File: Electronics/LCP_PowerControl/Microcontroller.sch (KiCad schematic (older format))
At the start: 22 parts, among them J4 Conn_02x02_Odd_Even, J5 Conn_02x05_Odd_Even, J6 Conn_02x06_Odd_Even, J7 Conn_02x02_Odd_Even, J8 Conn_02x02_Odd_Even, SW1 SW_Push, U3 MSP430FR5989, Y1 32.768kHz

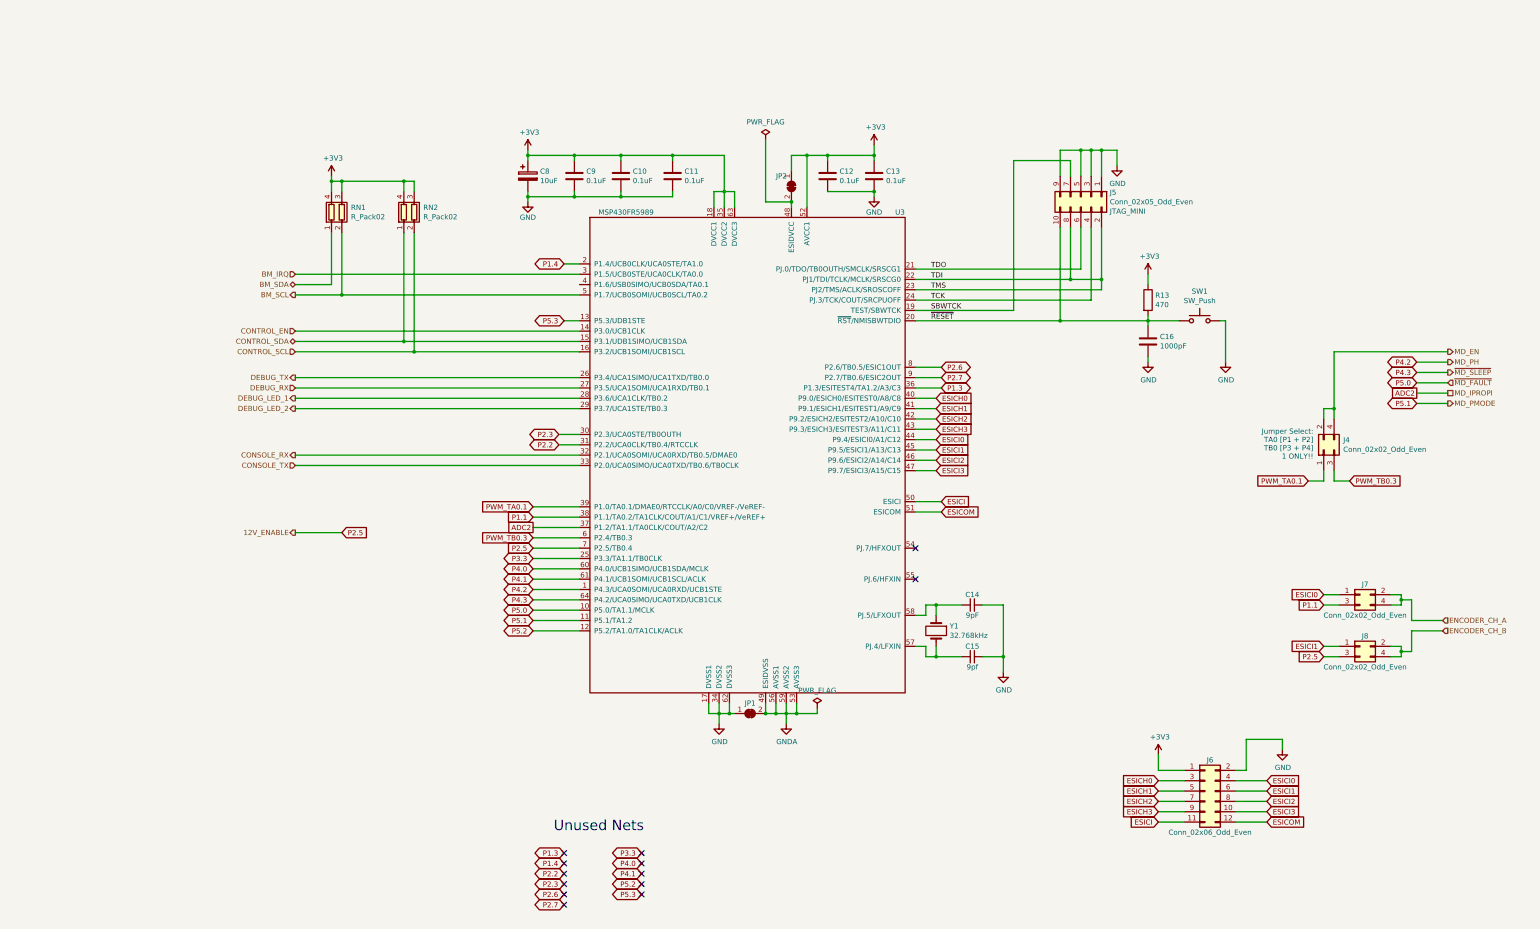
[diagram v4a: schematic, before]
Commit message: Rev1
Removed test points. Cleaned up unnecessary traces. Fixed electrical issues #1-#7
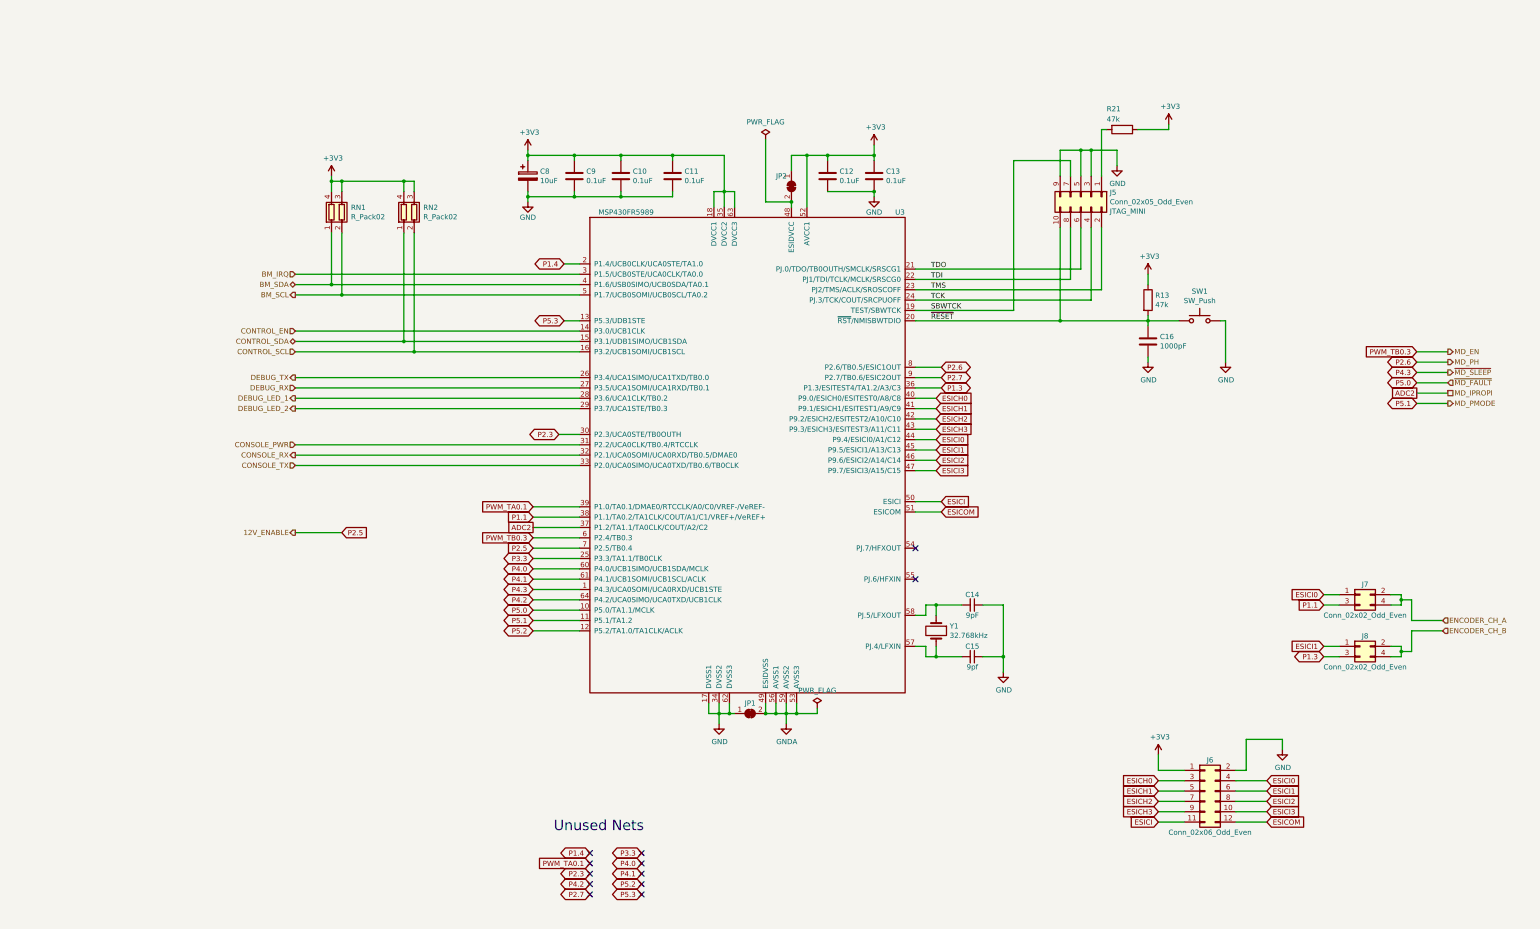
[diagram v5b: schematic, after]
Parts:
- removed J4: Conn_02x02_Odd_Even, Connector_PinHeader_2.00mm:PinHeader_2x02_P2.00mm_Vertical, symbol Connector_Generic:Conn_02x02_Odd_Even
- added R21: 47k, Resistor_SMD:R_0805_2012Metric, symbol Device:R
- R13: value 470 -> 47k; MPN CRGCQ0805F470R -> CRGCQ0805F47K
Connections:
- net +3V3: now also R21.1
- net BM_SDA: now also U3.4 (P1.6/USB0SIMO/UCB0SDA/TA0.1)
- net GND: no longer J5.1 (Pin_1)
- net P1.3: now also J8.3 (Pin_3)
- net P2.5: no longer J8.3 (Pin_3)
- net P4.2: now also U3.64 (P4.2/UCA0SIMO/UCA0TXD/UCB1CLK); no longer U3.1 (P4.3/UCA0SOMI/UCA0RXD/UCB1STE)
- net P4.3: now also U3.1 (P4.3/UCA0SOMI/UCA0RXD/UCB1STE); no longer U3.64 (P4.2/UCA0SIMO/UCA0TXD/UCB1CLK)
- net TDI: no longer J5.2 (Pin_2), U3.23 (PJ2/TMS/ACLK/SROSCOFF)
- net P2.2 renamed CONSOLE_PWR
- new net: J5.1 (Pin_1), R21.2
- new net TMS: J5.2 (Pin_2), U3.23 (PJ2/TMS/ACLK/SROSCOFF)
- no-connect marks 13 -> 12
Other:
- note removed: "Jumper Select:\nTA0 [P1 + P2]\nTB0 [P3 + P4]\n1 ONLY!!"
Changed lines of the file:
@@
 	11850 1850 11850 2000
-Wire Wire Line
-	11700 2100 11700 1850
-Connection ~ 11700 1850
-Wire Wire Line
-	11700 1850 11850 1850
 Wire Wire Line
 	11600 2100 11600 1850
@@
 	11300 1850 11500 1850
 Connection ~ 11600 1850
-Wire Wire Line
-	11600 1850 11700 1850
 Connection ~ 11500 1850
 Wire Wire Line
@@
 P 12150 3300
 F 0 "R13" H 12220 3346 50  0000 L CNN
-F 1 "470" H 12220 3255 50  0000 L CNN
+F 1 "47k" H 12220 3255 50  0000 L CNN
 F 2 "Resistor_SMD:R_0805_2012Metric" V 12080 3300 50  0001 C CNN
 F 3 "~" H 12150 3300 50  0001 C CNN
-F 4 "CRGCQ0805F470R" H 12150 3300 50  0001 C CNN "MPN"
+F 4 "CRGCQ0805F47K" H 12150 3300 50  0001 C CNN "MPN"
 	1    12150 3300
 	1    0    0    -1
@@
 Text GLabel 6200 6000 0    50   BiDi ~ 0
 P4.1
+Text GLabel 6200 6200 0    50   BiDi ~ 0
+P4.2
 Text GLabel 6200 6100 0    50   BiDi ~ 0
-P4.2
-Text GLabel 6200 6200 0    50   BiDi ~ 0
 P4.3
 Wire Wire Line
@@
 Wire Wire Line
 	6200 6300 6650 6300
-Text GLabel 14750 3900 0    50   BiDi ~ 0
+Text GLabel 6750 8950 0    50   BiDi ~ 0
 P4.2
 Wire Wire Line
@@
 Wire Wire Line
 	6200 5500 6650 5500
-Wire Wire Line
-	13850 4350 13950 4350
-Connection ~ 13950 4350
-Wire Wire Line
-	13950 3800 13950 4350
-Wire Wire Line
-	13950 3800 15050 3800
-Text GLabel 13700 5050 0    50   Input ~ 0
-PWM_TA0.1
-Wire Wire Line
-	13700 5050 13850 5050
-Wire Wire Line
-	13850 5050 13850 4950
-$Comp
-L Connector_Generic:Conn_02x02_Odd_Even J4
-U 1 1 5EFC98B3
-P 13850 4750
-F 0 "J4" V 13946 4562 50  0000 R CNN
-F 1 "Conn_02x02_Odd_Even" V 13855 4562 50  0000 R CNN
-F 2 "Connector_PinHeader_2.00mm:PinHeader_2x02_P2.00mm_Vertical" H 13850 4750 50  0001 C CNN
-F 3 "~" H 13850 4750 50  0001 C CNN
-	1    13850 4750
-	0    -1   -1   0
-$EndComp
-Wire Wire Line
-	13950 4350 13950 4450
-Wire Wire Line
-	13850 4350 13850 4450
-Text GLabel 14100 5050 2    50   Input ~ 0
+Text GLabel 14750 3800 0    50   Input ~ 0
 PWM_TB0.3
-Wire Wire Line
-	14100 5050 13950 5050
-Wire Wire Line
-	13950 5050 13950 4950
-Text Notes 13750 4850 2    50   ~ 0
-Jumper Select:\nTA0 [P1 + P2]\nTB0 [P3 + P4]\n1 ONLY!!
 Text GLabel 14750 4200 0    50   UnSpc ~ 0
 ADC2
@@
 Wire Wire Line
 	13850 6250 14000 6250
-Text GLabel 13850 6750 0    50   Input ~ 0
-P2.5
-Wire Wire Line
-	13850 6750 14000 6750
 Text GLabel 4350 5550 2    50   Input ~ 0
 P2.5
@@
 Text GLabel 7250 9050 0    50   BiDi ~ 0
 P5.3
-Text GLabel 6500 8750 0    50   BiDi ~ 0
+Text GLabel 6750 8650 0    50   BiDi ~ 0
 P1.4
 Text GLabel 10150 3950 2    50   BiDi ~ 0
@@
 Wire Wire Line
 	10150 3950 9900 3950
-Text GLabel 6500 9050 0    50   BiDi ~ 0
+Text GLabel 14750 3900 0    50   BiDi ~ 0
 P2.6
-Text GLabel 6500 9150 0    50   BiDi ~ 0
+Text GLabel 6750 9050 0    50   BiDi ~ 0
 P2.7
-Text GLabel 6500 8650 0    50   BiDi ~ 0
+Text GLabel 13850 6750 0    50   BiDi ~ 0
 P1.3
-Text GLabel 6450 4700 0    50   BiDi ~ 0
-P2.2
 Text GLabel 6450 4600 0    50   BiDi ~ 0
 P2.3
 Wire Wire Line
 	6650 4600 6450 4600
-Wire Wire Line
-	6650 4700 6450 4700
-Text GLabel 6500 8850 0    50   BiDi ~ 0
-P2.2
-Text GLabel 6500 8950 0    50   BiDi ~ 0
+Text GLabel 6750 8850 0    50   BiDi ~ 0
 P2.3
 Text GLabel 6200 5800 0    50   BiDi ~ 0
@@
 Text GLabel 7250 8650 0    50   BiDi ~ 0
 P3.3
-NoConn ~ 6500 8650
-NoConn ~ 6500 8750
-NoConn ~ 6500 8850
-NoConn ~ 6500 8950
-NoConn ~ 6500 9050
-NoConn ~ 6500 9150
+NoConn ~ 6750 8650
+NoConn ~ 6750 8850
+NoConn ~ 6750 8950
+NoConn ~ 6750 9050
 NoConn ~ 7250 9050
 NoConn ~ 7250 8950
@@
 Connection ~ 8750 7300
 Wire Wire Line
-	11700 3100 11700 2600
-Wire Wire Line
-	11700 3200 11700 3100
-Connection ~ 11700 3100
-Connection ~ 11400 3100
-Wire Wire Line
-	11400 3100 11700 3100
+	11700 3200 11700 2600
+Wire Wire Line
+	11600 1850 11850 1850
+$Comp
+L Device:R R21
+U 1 1 5FE87C7E
+P 11900 1650
+F 0 "R21" V 11700 1500 50  0000 L CNN
+F 1 "47k" V 11800 1500 50  0000 L CNN
+F 2 "Resistor_SMD:R_0805_2012Metric" V 11830 1650 50  0001 C CNN
+F 3 "~" H 11900 1650 50  0001 C CNN
+F 4 "CRGCQ0805F470R" H 11900 1650 50  0001 C CNN "MPN"
+	1    11900 1650
+	0    1    1    0
+$EndComp
+Wire Wire Line
+	11750 1650 11700 1650
+Wire Wire Line
+	11700 1650 11700 2100
+$Comp
+L power:+3V3 #PWR015
+U 1 1 5FE93D4D
+P 12350 1600
+F 0 "#PWR015" H 12350 1450 50  0001 C CNN
+F 1 "+3V3" H 12365 1773 50  0000 C CNN
+F 2 "" H 12350 1600 50  0001 C CNN
+F 3 "" H 12350 1600 50  0001 C CNN
+	1    12350 1600
+	1    0    0    -1
+$EndComp
+Wire Wire Line
+	12050 1650 12350 1650
+Wire Wire Line
+	12350 1650 12350 1600
+Wire Wire Line
+	3900 4700 6650 4700
+Wire Wire Line
+	6650 3150 4250 3150
+Connection ~ 4250 3150
+Wire Wire Line
+	13850 6750 14000 6750
+Wire Wire Line
+	14750 3800 15050 3800
+Text HLabel 3900 4700 0    50   Input ~ 0
+CONSOLE_PWR
+Text GLabel 6750 8750 0    50   Input ~ 0
+PWM_TA0.1
+NoConn ~ 6750 8750
 $EndSCHEMATC

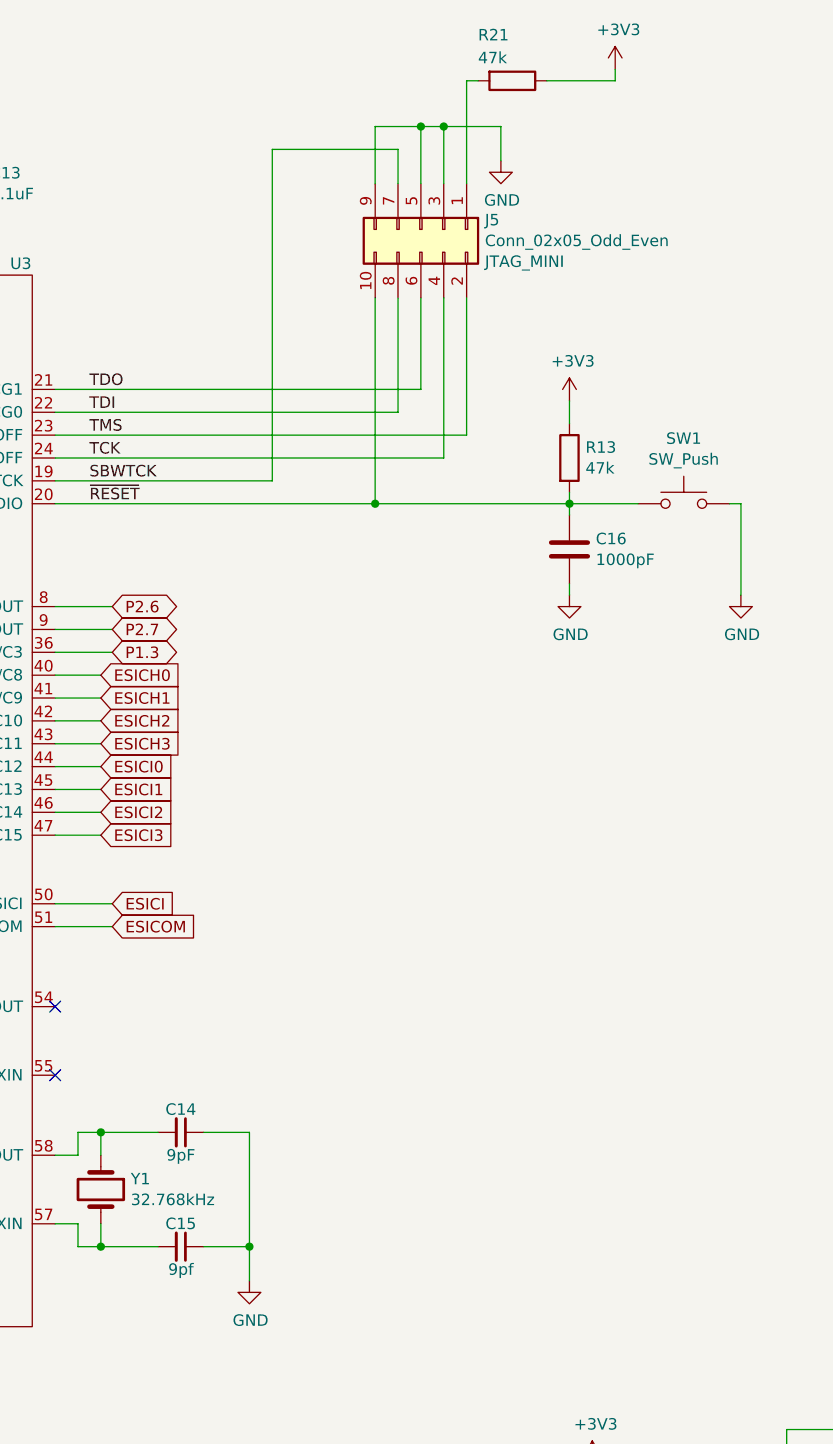
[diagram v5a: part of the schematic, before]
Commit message: BOM Update
Updated MPNs on components to match supplies as well as correcting some resistor values
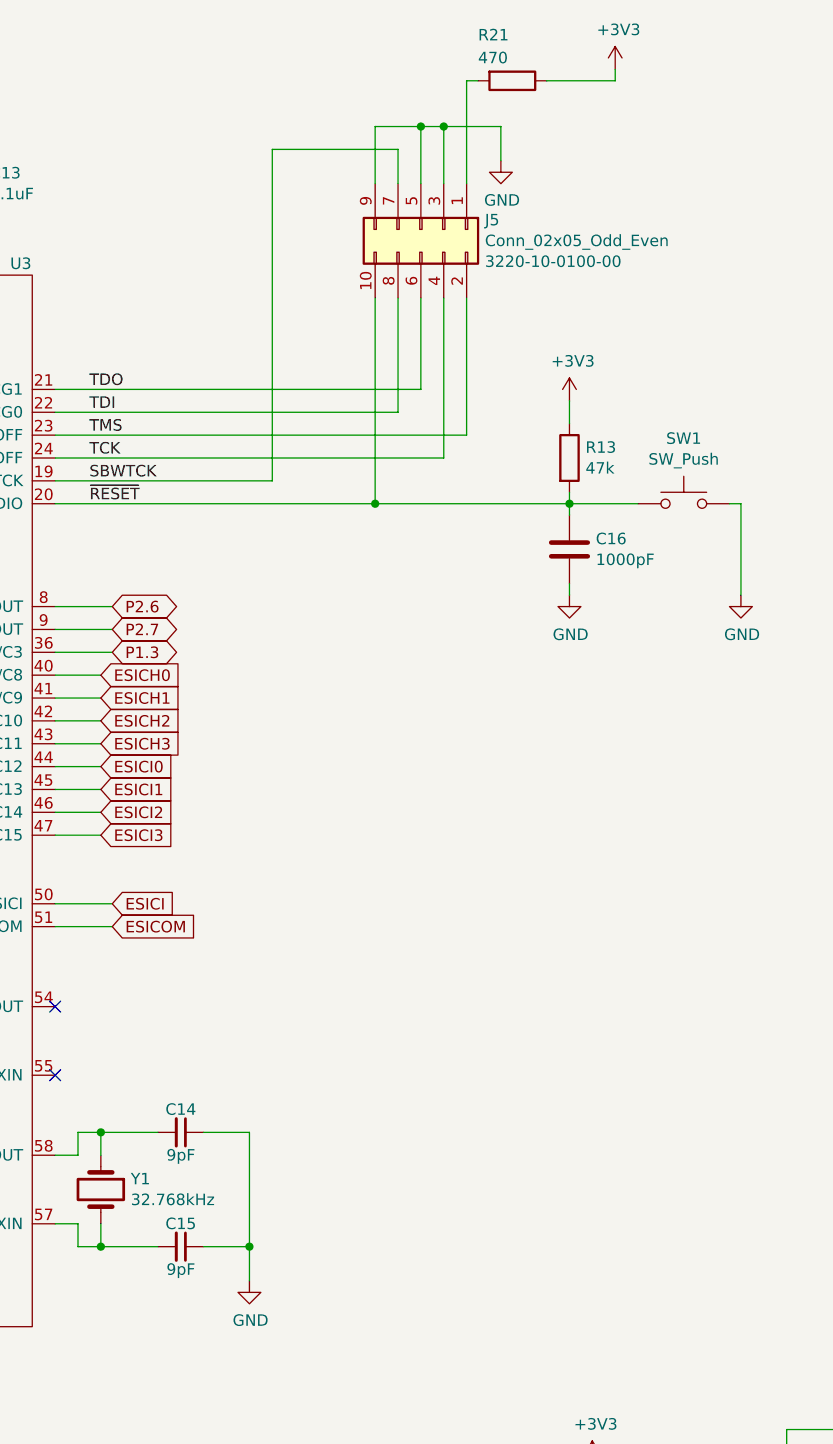
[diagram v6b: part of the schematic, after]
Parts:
- C15: value 9pf -> 9pF
- J5: Field4 JTAG_MINI -> (none); MPN (none) -> 3220-10-0100-00
- J6: MPN (none) -> 2842126-6
- J7, J8: MPN (none) -> 5176264-1
- R21: value 47k -> 470
- Y1: Field4 ABS07-32.768KHZ-9-T -> (none); MPN (none) -> ABS07-32.768KHZ-9-T
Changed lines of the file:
@@
 F 2 "Connector_PinSocket_1.27mm:PinSocket_2x05_P1.27mm_Vertical" H 11500 2300 50  0001 C CNN
 F 3 "~" H 11500 2300 50  0001 C CNN
-F 4 "JTAG_MINI" V 11641 2580 50  0000 L CNN "Field4"
+F 4 "3220-10-0100-00" V 11641 2580 50  0000 L CNN "MPN"
 	1    11500 2300
 	0    1    1    0
@@
 F 2 "Crystal:Crystal_SMD_3215-2Pin_3.2x1.5mm" H 10100 6500 50  0001 C CNN
 F 3 "~" H 10100 6500 50  0001 C CNN
-F 4 "ABS07-32.768KHZ-9-T" V 10100 6500 50  0001 C CNN "Field4"
+F 4 "ABS07-32.768KHZ-9-T" V 10100 6500 50  0001 C CNN "MPN"
 	1    10100 6500
 	0    1    1    0
@@
 P 10450 6750
 F 0 "C15" V 10350 6750 50  0000 C CNN
-F 1 "9pf" V 10550 6750 50  0000 C CNN
+F 1 "9pF" V 10550 6750 50  0000 C CNN
 F 2 "Capacitor_SMD:C_0603_1608Metric" H 10450 6750 50  0001 C CNN
 F 3 "~" H 10450 6750 50  0001 C CNN
@@
 F 2 "Connector_PinHeader_2.00mm:PinHeader_2x06_P2.00mm_Vertical" H 12700 8050 50  0001 C CNN
 F 3 "~" H 12700 8050 50  0001 C CNN
+F 4 "2842126-6" H 12700 8050 50  0001 C CNN "MPN"
 	1    12700 8050
 	1    0    0    -1
@@
 F 2 "Connector_PinHeader_2.00mm:PinHeader_2x02_P2.00mm_Vertical" H 14200 6150 50  0001 C CNN
 F 3 "~" H 14200 6150 50  0001 C CNN
+F 4 "5176264-1" H 14200 6150 50  0001 C CNN "MPN"
 	1    14200 6150
 	1    0    0    -1
@@
 F 2 "Connector_PinHeader_2.00mm:PinHeader_2x02_P2.00mm_Vertical" H 14200 6650 50  0001 C CNN
 F 3 "~" H 14200 6650 50  0001 C CNN
+F 4 "5176264-1" H 14200 6650 50  0001 C CNN "MPN"
 	1    14200 6650
 	1    0    0    -1
@@
 Wire Wire Line
 	11600 1850 11850 1850
-$Comp
-L Device:R R21
-U 1 1 5FE87C7E
-P 11900 1650
-F 0 "R21" V 11700 1500 50  0000 L CNN
-F 1 "47k" V 11800 1500 50  0000 L CNN
-F 2 "Resistor_SMD:R_0805_2012Metric" V 11830 1650 50  0001 C CNN
-F 3 "~" H 11900 1650 50  0001 C CNN
-F 4 "CRGCQ0805F470R" H 11900 1650 50  0001 C CNN "MPN"
-	1    11900 1650
-	0    1    1    0
-$EndComp
-Wire Wire Line
-	11750 1650 11700 1650
 Wire Wire Line
 	11700 1650 11700 2100
@@
 $EndComp
 Wire Wire Line
-	12050 1650 12350 1650
-Wire Wire Line
-	12350 1650 12350 1600
-Wire Wire Line
 	3900 4700 6650 4700
 Wire Wire Line
@@
 PWM_TA0.1
 NoConn ~ 6750 8750
+Wire Wire Line
+	12350 1650 12350 1600
+Wire Wire Line
+	11750 1650 11700 1650
+Wire Wire Line
+	12050 1650 12350 1650
+$Comp
+L Device:R R21
+U 1 1 5FE87C7E
+P 11900 1650
+F 0 "R21" V 11700 1500 50  0000 L CNN
+F 1 "470" V 11800 1500 50  0000 L CNN
+F 2 "Resistor_SMD:R_0805_2012Metric" V 11830 1650 50  0001 C CNN
+F 3 "~" H 11900 1650 50  0001 C CNN
+F 4 "CRGCQ0805F470R" H 11900 1650 50  0001 C CNN "MPN"
+	1    11900 1650
+	0    1    1    0
+$EndComp
 $EndSCHEMATC
